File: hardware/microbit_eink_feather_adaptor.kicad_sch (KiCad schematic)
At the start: 3 parts, among them J1 feather long, J2 feather short, J3 microbit_edge_connector

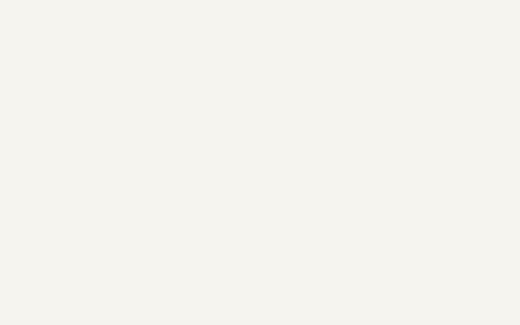
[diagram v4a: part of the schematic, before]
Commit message: pcb: Replace butterfly hole with custom footprint.
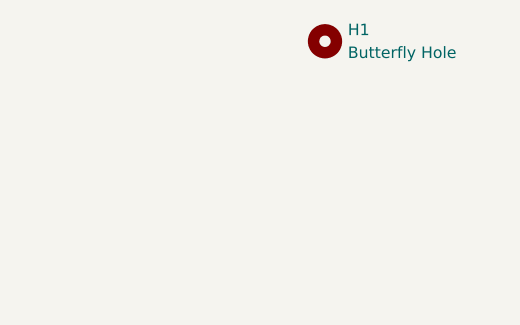
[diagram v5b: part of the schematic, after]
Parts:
- added H1: Butterfly Hole, project_library:butterfly_hole, symbol Mechanical:MountingHole
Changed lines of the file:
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@@
     (pin "1")
+  )
+  (symbol (lib_id "Mechanical:MountingHole") (at 260.35 25.4 0) (unit 1)
+    (in_bom yes) (on_board yes) (fields_autoplaced)
+    (property "Reference" "H1" (id 0) (at 262.89 24.1299 0)
+      (effects (font (size 1.27 1.27)) (justify left))
+    )
+    (property "Value" "Butterfly Hole" (id 1) (at 262.89 26.6699 0)
+      (effects (font (size 1.27 1.27)) (justify left))
+    )
+    (property "Footprint" "project_library:butterfly_hole" (id 2) (at 260.35 25.4 0)
+      (effects (font (size 1.27 1.27)) hide)
+    )
+    (property "Datasheet" "~" (id 3) (at 260.35 25.4 0)
+      (effects (font (size 1.27 1.27)) hide)
+    )
   )
   (symbol (lib_id "lib_microbit_connector:microbit_edge_connector") (at 185.42 90.17 0) (mirror y) (unit 1)
@@
       (reference "#PWR02") (unit 1) (value "GND") (footprint "")
     )
+    (path "/8b377121-a72a-4f01-aeea-1bf170c0c95b"
+      (reference "H1") (unit 1) (value "Butterfly Hole") (footprint "project_library:butterfly_hole")
+    )
     (path "/00000000-0000-0000-0000-00005d375c76"

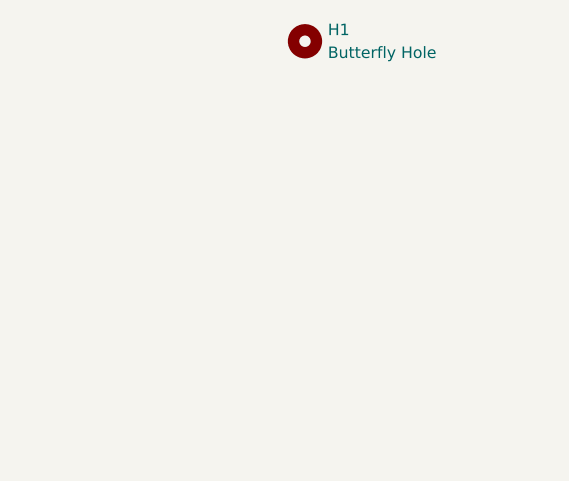
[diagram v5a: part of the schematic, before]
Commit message: schematic & pcb: Add (optional) header to physically hold battery.
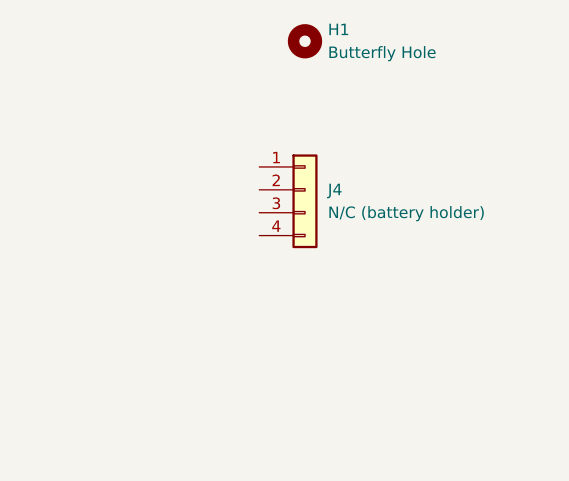
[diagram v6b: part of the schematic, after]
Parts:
- added J4: N/C (battery holder), Connector_PinHeader_2.54mm:PinHeader_1x04_P2.54mm_Vertical, symbol Connector_Generic:Conn_01x04
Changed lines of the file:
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@@
   (title_block
     (title "micro:bit eInk FeatherWing Adaptor")
-    (date "2022-06-26")
+    (date "2022-06-27")
     (rev "V1.1")
   )
@@
     (pin "9")
   )
+  (symbol (lib_id "Connector_Generic:Conn_01x04") (at 260.35 41.91 0) (unit 1)
+    (in_bom yes) (on_board yes) (fields_autoplaced)
+    (property "Reference" "J4" (id 0) (at 262.89 41.9099 0)
+      (effects (font (size 1.27 1.27)) (justify left))
+    )
+    (property "Value" "N/C (battery holder)" (id 1) (at 262.89 44.4499 0)
+      (effects (font (size 1.27 1.27)) (justify left))
+    )
+    (property "Footprint" "Connector_PinHeader_2.54mm:PinHeader_1x04_P2.54mm_Vertical" (id 2) (at 260.35 41.91 0)
+      (effects (font (size 1.27 1.27)) hide)
+    )
+    (property "Datasheet" "~" (id 3) (at 260.35 41.91 0)
+      (effects (font (size 1.27 1.27)) hide)
+    )
+    (pin "1")
+    (pin "2")
+    (pin "3")
+    (pin "4")
+  )
   (sheet_instances
     (path "/" (page "1"))
@@
       (reference "J3") (unit 1) (value "microbit_edge_connector") (footprint "Connector_PCBEdge:4UCON_10156_2x40_P1.27mm_Socket_Horizontal")
     )
-  )
+    (path "/fb976ca8-6508-4fdd-aef7-4dea66b3d3be"
+      (reference "J4") (unit 1) (value "N/C (battery holder)") (footprint "Connector_PinHeader_2.54mm:PinHeader_1x04_P2.54mm_Vertical")
+    )
+  )
